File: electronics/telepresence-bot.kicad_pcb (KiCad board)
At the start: 4 copper layers, 100 x 100 mm, 191 parts, among them J1 STATUS, J10 Conn_01x02_Pin, J12 GND, J13 Conn_01x08_Pin, J14 IOLV / VIO, J15 Conn_02x06_Counter_Clockwise, J16 MOT_CON, J17 Conn_02x06_Counter_Clockwise, J18 MOT_CON, J19 Conn_02x06_Counter_Clockwise, J2 EXT_PWR_BTN, J20 MOT_CON, J3 IOLV_IN, J4 BATT, J5 BATT_OUT, J6 Conn_02x06_Counter_Clockwise, J7 MOT_CON, J8 VMOT, J9 BP_MOTOR_ENABLE, Q1 Q_PMOS_GDS, Q2 PMOS_GDS, Q3 2N3904, Q4 2N3904, U10 ISO7762DBQ, U11 LM1117DT-3.3, U12 SFH617A-1, U13 BTT TMC5160 Pro, U14 BTT TMC5160 Pro, U15 BTT TMC5160 Pro, U2 LM1117DT-5.0, U3 LM1117DT-3.3, U4 SFH617A-1, U5 DBG_HDR, U6 INA228, U7 BTT TMC5160 Pro, U8 SFH617A-1, U9 74LVC125

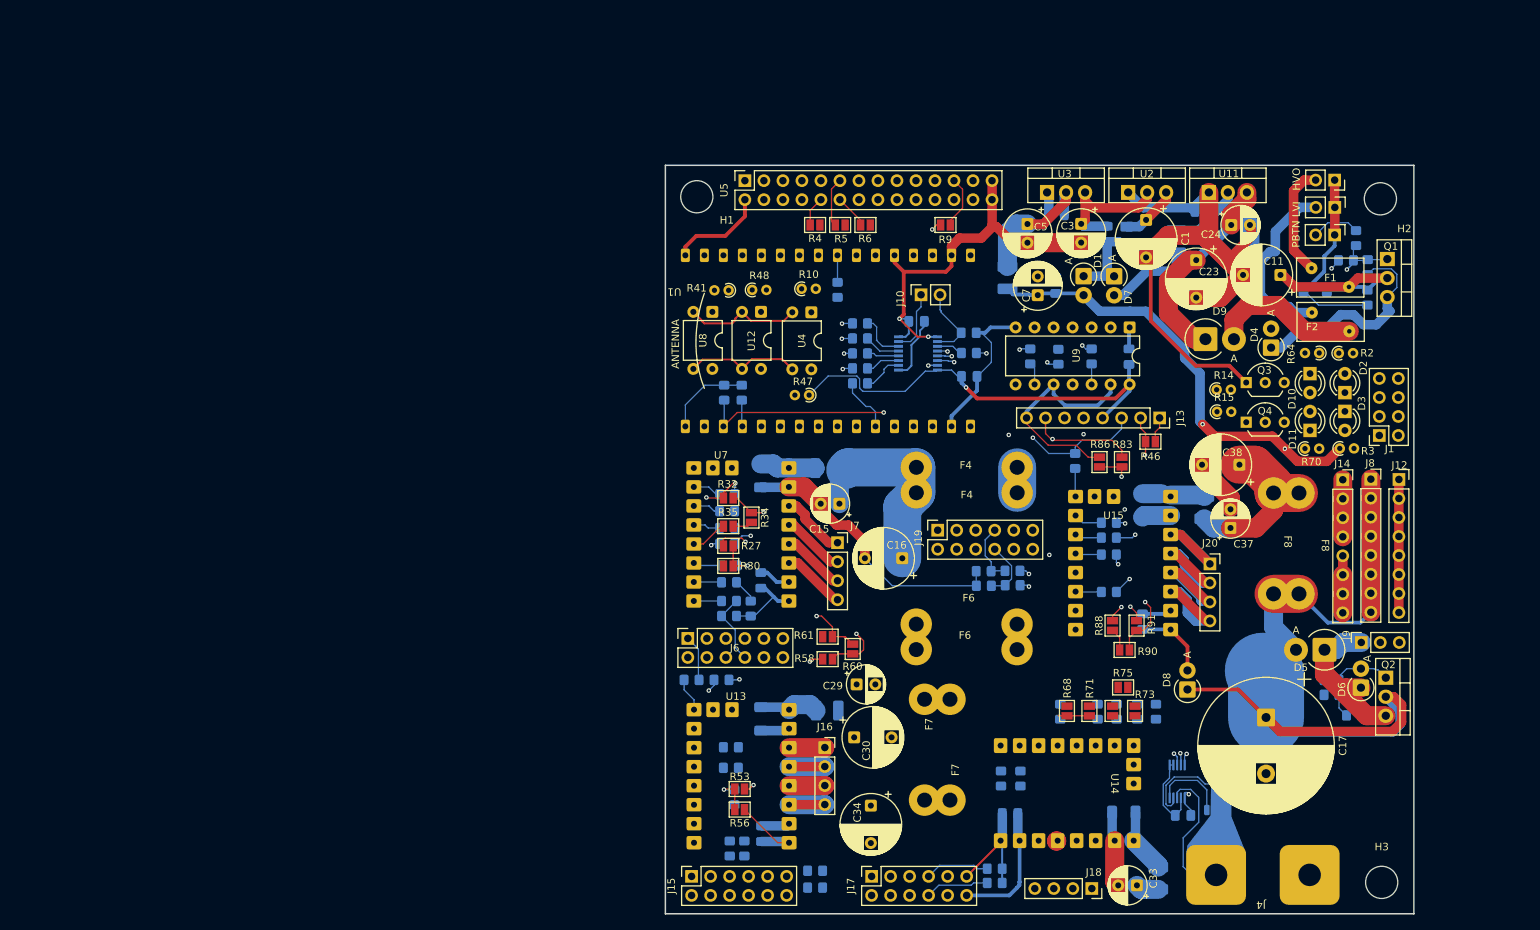
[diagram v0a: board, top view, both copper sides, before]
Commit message: Switching to a bigger PCB since cost seems negligible
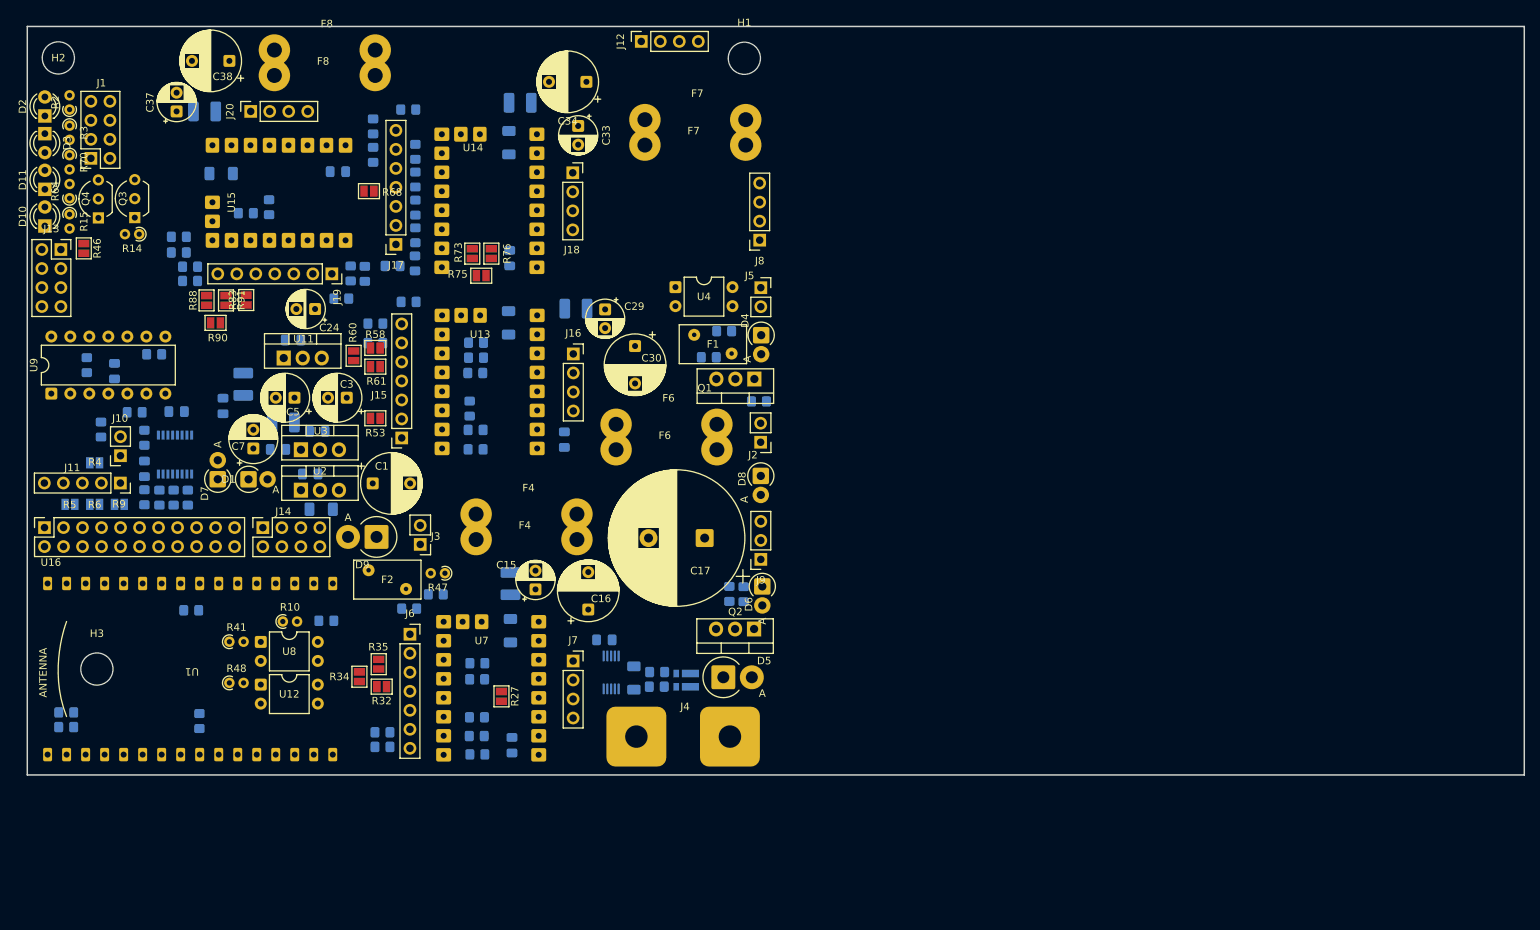
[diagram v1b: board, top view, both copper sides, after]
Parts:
- removed C11, C23: 100uF, Capacitor_THT:CP_Radial_D8.0mm_P5.00mm
- removed C12: 100nF, Capacitor_SMD:C_1206_3216Metric_Pad1.33x1.80mm_HandSolder
- removed R56, R71, R86: 0, Jumper:SolderJumper-2_P1.3mm_Open_Pad1.0x1.5mm
- removed U5: DBG_HDR, Connector_PinSocket_2.54mm:PinSocket_2x14_P2.54mm_Vertical
- added C10: 100nF, Capacitor_SMD:C_1206_3216Metric_Pad1.33x1.80mm_HandSolder, B.Cu at (146.3, 118.5)
- added J11: DRIVER_GPIO, Connector_PinSocket_2.54mm:PinSocket_1x05_P2.54mm_Vertical, F.Cu at (77.7, 92.5)
- added U16: DBG_HDR, Connector_PinSocket_2.54mm:PinSocket_2x11_P2.54mm_Vertical, F.Cu at (67.5, 98.4)
- J12, J8: footprint Connector_PinSocket_2.54mm:PinSocket_1x08_P2.54mm_Vertical -> Connector_PinSocket_2.54mm:PinSocket_1x04_P2.54mm_Vertical
- J13, J14: footprint Connector_PinSocket_2.54mm:PinSocket_1x08_P2.54mm_Vertical -> Connector_PinSocket_2.54mm:PinSocket_2x04_P2.54mm_Vertical
- J15, J17, J19, J6: value Conn_02x06_Counter_Clockwise -> Conn_01x07_Pin; footprint Connector_PinSocket_2.54mm:PinSocket_2x06_P2.54mm_Vertical -> Connector_PinSocket_2.54mm:PinSocket_1x07_P2.54mm_Vertical
- R12: value 100k -> 33R
- R22: footprint Resistor_SMD:R_Shunt_Vishay_WSK2512_6332Metric_T2.66mm -> Resistor_SMD:R_Shunt_Vishay_WSKW0612
- R30: value 0 -> 33R; footprint Jumper:SolderJumper-2_P1.3mm_Open_Pad1.0x1.5mm -> Resistor_SMD:R_0805_2012Metric_Pad1.20x1.40mm_HandSolder; moved to B.Cu
- R4, R5, R6, R9: moved to B.Cu
- moved H2 177.6 mm to (69.4, 35.6)
- moved D3 177.6 mm to (67.6, 45.8)
- moved D2 177.6 mm to (67.6, 43.4)
- moved J1 176.1 mm to (73.8, 49.1)
- moved R3 175.1 mm to (70.9, 44.7), turned to -90 degrees
- moved H3 174.0 mm to (74.5, 117.3)
- moved R2 172.7 mm to (70.9, 42.5), turned to 90 degrees
- moved D11 172.1 mm to (67.6, 53.2)
- moved D10 170.2 mm to (67.6, 58.1), turned to 90 degrees
- moved R70 169.6 mm to (70.9, 48.6), turned to -90 degrees
- moved R64 168.2 mm to (70.9, 54.4), turned to 90 degrees
- moved Q4 155.8 mm to (74.8, 57.0), turned to 90 degrees
- moved R15 155.6 mm to (70.9, 56.5), turned to -90 degrees
- moved C37 151.4 mm to (85.2, 42.8)
- moved Q3 150.1 mm to (79.6, 57.0), turned to 90 degrees
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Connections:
- J15 pad 1: /drivers/DRV_ENABLE_ISO -> /drivers/motor_driver/_CLK_DCO
- J15 pad 2: /drivers/motor_driver/_MOSI -> /drivers/motor_driver/_MISO
- J15 pad 3: /drivers/DRV_SCK_ISO -> Net-(J15-Pin_3)
- J15 pad 4: /drivers/DRV_CS_ISO -> Net-(J15-Pin_4)
- J15 pad 5: /drivers/motor_driver/_MISO -> /drivers/motor_driver/_MOSI
- J15 pad 6: /drivers/motor_driver/_CLK_DCO -> /drivers/motor_driver/_DIR
- J17 pad 1: /drivers/DRV_ENABLE_ISO -> /drivers/motor_driver2/_CLK_DCO
- J17 pad 2: /drivers/motor_driver2/_MOSI -> /drivers/motor_driver2/_MISO
- J17 pad 3: /drivers/DRV_SCK_ISO -> Net-(J17-Pin_3)
- J17 pad 4: /drivers/DRV_CS_ISO -> Net-(J17-Pin_4)
- J17 pad 5: /drivers/motor_driver2/_MISO -> /drivers/motor_driver2/_MOSI
- J17 pad 6: /drivers/motor_driver2/_CLK_DCO -> /drivers/motor_driver2/_DIR
- J19 pad 1: /drivers/DRV_ENABLE_ISO -> /drivers/motor_driver3/_CLK_DCO
- J19 pad 2: /drivers/motor_driver3/_MOSI -> /drivers/motor_driver3/_MISO
- J19 pad 3: /drivers/DRV_SCK_ISO -> Net-(J19-Pin_3)
- J19 pad 4: /drivers/DRV_CS_ISO -> Net-(J19-Pin_4)
- J19 pad 5: /drivers/motor_driver3/_MISO -> /drivers/motor_driver3/_MOSI
- J19 pad 6: /drivers/motor_driver3/_CLK_DCO -> /drivers/motor_driver3/_DIR
- J6 pad 1: /drivers/DRV_ENABLE_ISO -> /drivers/motor_driver1/_CLK_DCO
- J6 pad 2: /drivers/motor_driver1/_MOSI -> /drivers/motor_driver1/_MISO
- J6 pad 3: /drivers/DRV_SCK_ISO -> Net-(J6-Pin_3)
- J6 pad 4: /drivers/DRV_CS_ISO -> Net-(J6-Pin_4)
- J6 pad 5: /drivers/motor_driver1/_MISO -> /drivers/motor_driver1/_MOSI
- J6 pad 6: /drivers/motor_driver1/_CLK_DCO -> /drivers/motor_driver1/_DIR
- R12 pad 1: /AUX_PWR_RAIL -> Net-(U6-Vin+)
- R12 pad 2: GND -> Net-(R12-Pad2)
- R22 pad 1: +BATT -> /MOTOR_POWER_RAIL
- R22 pad 2: Net-(U6-Vin+) -> Net-(R22-Pad2)
- R22 pad 3: Net-(U6-Vin-) -> Net-(R12-Pad2)
- R22 pad 4: /MOTOR_POWER_RAIL -> +BATT
- R30 pad 1: GND -> Net-(U6-Vin-)
- R30 pad 2: /drivers/motor_driver1/_CLK_DCO -> Net-(R22-Pad2)
- U13 pad 17: Net-(J15-Pin_9) -> Net-(J15-Pin_4)
- U13 pad 18: Net-(J15-Pin_10) -> Net-(J15-Pin_3)
- U14 pad 17: Net-(J17-Pin_9) -> Net-(J17-Pin_4)
- U14 pad 18: Net-(J17-Pin_10) -> Net-(J17-Pin_3)
- U15 pad 17: Net-(J19-Pin_9) -> Net-(J19-Pin_4)
- U15 pad 18: Net-(J19-Pin_10) -> Net-(J19-Pin_3)
- U7 pad 17: Net-(J6-Pin_9) -> Net-(J6-Pin_4)
- U7 pad 18: Net-(J6-Pin_10) -> Net-(J6-Pin_3)
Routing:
- net GND: track 457.1 -> 0.00 mm, vias 2 -> 0
- net /3v3_compute: track 148.0 -> 0.00 mm, vias 3 -> 0
- net VMOT: track 135.7 -> 0.00 mm
- net /drivers/DRV_CLK_ISO: track 134.1 -> 0.00 mm, vias 3 -> 0
- net /drivers/DRV_VIO_ISO: track 107.8 -> 0.00 mm, vias 1 -> 0
- net /SDA: track 104.5 -> 0.00 mm, vias 3 -> 0
- net /drivers/DRV_ENABLE_ISO: track 101.8 -> 0.00 mm, vias 2 -> 0
- net /SCL: track 66.6 -> 0.00 mm, vias 1 -> 0
- net /drivers/DRV_MOSI_ISO: track 59.3 -> 0.00 mm, vias 2 -> 0
- net /drivers/DRV_CS_ISO: track 57.1 -> 0.00 mm, vias 3 -> 0
- net /MOTOR_POWER_RAIL: track 50.9 -> 0.00 mm
- net /drivers/DRV_SCK_ISO: track 49.9 -> 0.00 mm, vias 2 -> 0
- net /drivers/motor_driver3/_CLK_DCO: track 47.3 -> 0.00 mm, vias 2 -> 0
- net /drivers/motor_driver3/_MOSI: track 41.0 -> 0.00 mm, vias 2 -> 0
- net /IOLV_IN: track 35.6 -> 0.00 mm
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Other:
- board size 100 x 100 mm -> 200 x 100 mm
- board text removed: "HVO"
- board text removed: "LVI"
- board text removed: "PBTN"

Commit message: Updating electronics CAD post-production
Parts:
- removed R73, R75, R76, R88, R90, R91: 0, Jumper:SolderJumper-2_P1.3mm_Open_Pad1.0x1.5mm
- added C11: 100uF, Capacitor_THT:CP_Radial_D6.3mm_P2.50mm, F.Cu at (62.5, 103.2)
- added C12: 100nF, Capacitor_SMD:C_0805_2012Metric_Pad1.18x1.45mm_HandSolder, B.Cu at (112.7, 102.2)
- added D12: D_Schottky, Diode_THT:D_DO-201AD_P5.08mm_Vertical_KathodeUp, F.Cu at (119.1, 77.7)
- added H4: MountingHole_Pad_MP, MountingHole:MountingHole_4.3mm_M4_ISO7380, F.Cu at (16.4, 107.8)
- added JP1: Jumper_2_Bridged, Connector_PinSocket_2.54mm:PinSocket_1x02_P2.54mm_Vertical, F.Cu at (109.2, 107.0)
- added JP2: Jumper_2_Bridged, Connector_PinSocket_2.54mm:PinSocket_1x02_P2.54mm_Vertical, F.Cu at (109.2, 79.1)
- added R56: 0, Jumper:SolderJumper-2_P1.3mm_Open_Pad1.0x1.5mm, B.Cu at (72.3, 57.4)
- D5, D9: footprint Diode_THT:D_DO-201AD_P3.81mm_Vertical_AnodeUp -> Diode_THT:D_DO-201AD_P5.08mm_Vertical_KathodeUp
- D8: footprint Diode_THT:D_DO-41_SOD81_P2.54mm_Vertical_AnodeUp -> Diode_THT:D_DO-201AD_P5.08mm_Vertical_KathodeUp
- R32, R34, R35, R58, R60, R61: moved to B.Cu
- R41, R47: footprint Resistor_THT:R_Axial_DIN0204_L3.6mm_D1.6mm_P1.90mm_Vertical -> Resistor_THT:R_Axial_DIN0204_L3.6mm_D1.6mm_P2.54mm_Vertical
- moved J8 147.9 mm to (22.5, 14.1), turned to 0 degrees
- moved D8 135.0 mm to (50.0, 18.1)
- moved J12 133.7 mm to (14.1, 22.4), turned to 0 degrees
- moved H3 116.6 mm to (16.4, 16.3)
- moved C17 113.2 mm to (77.1, 18.4), turned to -90 degrees
- moved F7 112.8 mm to (35.9, 29.8), turned to 90 degrees
- moved Q2 111.6 mm to (105.9, 15.7), turned to 0 degrees
- moved C16 108.3 mm to (65.2, 31.2)
- moved D5 107.7 mm to (111.7, 21.3), turned to 180 degrees
- moved J7 103.9 mm to (71.0, 36.9), turned to 90 degrees
- moved R38 103.2 mm to (108.6, 18.4), turned to 180 degrees
- moved R40 102.4 mm to (113.3, 15.6), turned to -90 degrees
- moved J9 100.4 mm to (115.6, 14.3), turned to 0 degrees
- moved R22 99.4 mm to (115.5, 26.8), turned to -90 degrees
- moved C13 97.3 mm to (81.5, 43.2), turned to 180 degrees
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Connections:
- C1 pad 1: /IOLV_IN -> Net-(D12-K)
- C2 pad 1: /IOLV_IN -> Net-(D12-K)
- J13 pad 5: /drivers/DRV_SCK_ISO -> Net-(J13-Pin_5)
- J13 pad 6: /drivers/DRV_CS_ISO -> Net-(J13-Pin_6)
- J13 pad 7: /drivers/DRV_CLK_ISO -> Net-(J13-Pin_7)
- J15 pad 1: /drivers/motor_driver/_CLK_DCO -> Net-(J15-Pin_1)
- J15 pad 2: /drivers/motor_driver/_MISO -> Net-(J15-Pin_2)
- J15 pad 3: Net-(J15-Pin_3) -> /drivers/DRV_MOSI_ISO
- J15 pad 4: Net-(J15-Pin_4) -> /drivers/motor_driver/_MISO
- J15 pad 5: /drivers/motor_driver/_MOSI -> /drivers/motor_driver/_CLK_DCO
- J15 pad 6: /drivers/motor_driver/_DIR -> /drivers/motor_driver/_STEP
- J15 pad 7: /drivers/motor_driver/_STEP -> /drivers/motor_driver/_DIR
- J17 pad 1: /drivers/motor_driver2/_CLK_DCO -> Net-(J17-Pin_1)
- J17 pad 2: /drivers/motor_driver2/_MISO -> Net-(J17-Pin_2)
- J17 pad 3: Net-(J17-Pin_3) -> /drivers/motor_driver1/_MISO
- J17 pad 4: Net-(J17-Pin_4) -> /drivers/motor_driver2/_MISO
- J17 pad 5: /drivers/motor_driver2/_MOSI -> /drivers/motor_driver2/_CLK_DCO
- J17 pad 6: /drivers/motor_driver2/_DIR -> /drivers/motor_driver2/_STEP
- J17 pad 7: /drivers/motor_driver2/_STEP -> /drivers/motor_driver2/_DIR
- J19 pad 1: /drivers/motor_driver3/_CLK_DCO -> Net-(J19-Pin_1)
- J19 pad 2: /drivers/motor_driver3/_MISO -> Net-(J19-Pin_2)
- J19 pad 3: Net-(J19-Pin_3) -> /drivers/motor_driver2/_MISO
- J19 pad 4: Net-(J19-Pin_4) -> /drivers/DRV_MOSI_LAST
- J19 pad 5: /drivers/motor_driver3/_MOSI -> /drivers/motor_driver3/_CLK_DCO
- J19 pad 6: /drivers/motor_driver3/_DIR -> /drivers/motor_driver3/_STEP
- J19 pad 7: /drivers/motor_driver3/_STEP -> /drivers/motor_driver3/_DIR
- J6 pad 1: /drivers/motor_driver1/_CLK_DCO -> Net-(J6-Pin_1)
- J6 pad 2: /drivers/motor_driver1/_MISO -> Net-(J6-Pin_2)
- J6 pad 3: Net-(J6-Pin_3) -> /drivers/motor_driver/_MISO
- J6 pad 4: Net-(J6-Pin_4) -> /drivers/motor_driver1/_MISO
- J6 pad 5: /drivers/motor_driver1/_MOSI -> /drivers/motor_driver1/_CLK_DCO
- J6 pad 6: /drivers/motor_driver1/_DIR -> /drivers/motor_driver1/_STEP
- J6 pad 7: /drivers/motor_driver1/_STEP -> /drivers/motor_driver1/_DIR
- R25 pad 1: /drivers/motor_driver1/_MOSI -> /drivers/motor_driver/_MISO
- R32 pad 1: /drivers/motor_driver/MISO -> /drivers/DRV_CLK_ISO
- R32 pad 2: /drivers/motor_driver1/_MOSI -> Net-(J13-Pin_7)
- R34 pad 1: /drivers/motor_driver/MISO -> /drivers/DRV_CS_ISO
- R34 pad 2: /drivers/motor_driver1/MISO -> Net-(J13-Pin_6)
- R35 pad 1: /drivers/motor_driver1/MISO -> /drivers/DRV_SCK_ISO
- R35 pad 2: /drivers/motor_driver1/_MISO -> Net-(J13-Pin_5)
- R36 pad 1: /drivers/motor_driver1/_STEP -> GND
- R36 pad 2: GND -> Net-(U7-STEP)
- R37 pad 1: /drivers/motor_driver1/_DIR -> GND
- R37 pad 2: GND -> Net-(U7-DIR)
- R51 pad 1: /drivers/motor_driver/_MOSI -> /drivers/DRV_MOSI_ISO
- R58 pad 2: /drivers/motor_driver/_MOSI -> /drivers/motor_driver/_MISO
- R60 pad 1: /drivers/DRV_MOSI_ISO -> /drivers/motor_driver1/_MISO
- R60 pad 2: /drivers/motor_driver/MISO -> /drivers/motor_driver2/_MISO
- R61 pad 1: /drivers/motor_driver/MISO -> /drivers/motor_driver2/_MISO
- R61 pad 2: /drivers/motor_driver/_MISO -> /drivers/DRV_MOSI_LAST
- R62 pad 1: /drivers/motor_driver/_STEP -> GND
- R62 pad 2: GND -> Net-(U13-STEP)
- R63 pad 1: /drivers/motor_driver/_DIR -> GND
- R63 pad 2: GND -> Net-(U13-DIR)
- R66 pad 1: /drivers/motor_driver2/_MOSI -> /drivers/motor_driver1/_MISO
- R77 pad 1: /drivers/motor_driver2/_STEP -> GND
- R77 pad 2: GND -> Net-(U14-STEP)
- R78 pad 1: /drivers/motor_driver2/_DIR -> GND
- R78 pad 2: GND -> Net-(U14-DIR)
- R81 pad 1: /drivers/motor_driver3/_MOSI -> /drivers/motor_driver2/_MISO
- R92 pad 1: /drivers/motor_driver3/_STEP -> GND
- R92 pad 2: GND -> Net-(U15-STEP)
- R93 pad 1: /drivers/motor_driver3/_DIR -> GND
- R93 pad 2: GND -> Net-(U15-DIR)
- U1 pad 1: /3v3_compute -> Net-(JP1-B)
- U1 pad 14: /5v_compute -> Net-(JP2-B)
- U13 pad 17: Net-(J15-Pin_4) -> Net-(J15-Pin_2)
- U13 pad 18: Net-(J15-Pin_3) -> Net-(J15-Pin_1)
- U14 pad 17: Net-(J17-Pin_4) -> Net-(J17-Pin_2)
- U14 pad 18: Net-(J17-Pin_3) -> Net-(J17-Pin_1)
- U15 pad 17: Net-(J19-Pin_4) -> Net-(J19-Pin_2)
- U15 pad 18: Net-(J19-Pin_3) -> Net-(J19-Pin_1)
- U15 pad 5: /drivers/motor_driver3/_MISO -> /drivers/DRV_MOSI_LAST
- U2 pad 3: /IOLV_IN -> Net-(D12-K)
- U7 pad 17: Net-(J6-Pin_4) -> Net-(J6-Pin_2)
- U7 pad 18: Net-(J6-Pin_3) -> Net-(J6-Pin_1)
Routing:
- net GND: track 0.00 -> 545.0 mm, vias 0 -> 98
- net /drivers/DRV_VIO_ISO: track 0.00 -> 249.0 mm, vias 0 -> 1
- net /3v3_compute: track 0.00 -> 232.4 mm, vias 0 -> 6
- net /5v_compute: track 0.00 -> 209.2 mm
- net /drivers/DRV_ENABLE_ISO: track 0.00 -> 137.7 mm, vias 0 -> 4
- net /drivers/DRV_SCK_ISO: track 0.00 -> 136.4 mm, vias 0 -> 6
- net /drivers/DRV_CS_ISO: track 0.00 -> 135.0 mm, vias 0 -> 6
- net /drivers/DRV_CLK_ISO: track 0.00 -> 124.6 mm, vias 0 -> 7
- net /IOLV_IN: track 0.00 -> 119.0 mm, vias 0 -> 1
- net /SDA: track 0.00 -> 114.5 mm, vias 0 -> 1
- net /SCL: track 0.00 -> 109.8 mm, vias 0 -> 2
- net /MOTOR_POWER_RAIL: track 0.00 -> 95.7 mm
- net /BATT_ALERT: track 0.00 -> 95.6 mm, vias 0 -> 3
- net VMOT: track 0.00 -> 84.0 mm
- net Net-(D6-A): track 0.00 -> 80.4 mm, vias 0 -> 1
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- added copper zone on B.Cu, net +BATT
- added copper zone on F.Cu, net +BATT
- added copper zone on In1.Cu, net +BATT
- added copper zone on In2.Cu, net +BATT
- added copper zone on B.Cu, net /MOTOR_POWER_RAIL
- added copper zone on F.Cu, net /MOTOR_POWER_RAIL
- added copper zone on In1.Cu, net /MOTOR_POWER_RAIL
- added copper zone on In2.Cu, net /MOTOR_POWER_RAIL
- added copper zone on B.Cu, net GND
- added copper zone on F.Cu, net GND
- added copper zone on In1.Cu, net GND
- added copper zone on In2.Cu, net GND
- added copper zone on B.Cu, net VMOT
- added copper zone on F.Cu, net VMOT
- added copper zone on In1.Cu, net VMOT
- added copper zone on In2.Cu, net VMOT
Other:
- board size 200 x 100 mm -> 116 x 100 mm
- board text added: "3v3 DRV GND 5v0 GND 5v0 5v0 HVE"
- board text added: "3v3 ISOLATE"
- board text added: "3v3 PWR"
- board text added: "5V-ISOLATE"
- board text added: "5v PWR"
- board text added: "AUX"
- board text added: "BP_0"
- board text added: "BP_1"
- board text added: "BP_2"
- board text added: "BP_3"
- board text added: "CLK DBG"
- board text added: "CLK_DBG"
- board text added: "CS_DBG CLK_DBG SCK_DBG"
- board text added: "DRV EN"
- board text added: "DRV0"
- board text added: "DRV1"
- board text added: "DRV2"
- board text added: "DRV3"
- board text added: "ESP32 C6 DevKitC v1"
- board text added: "GND"
- board text added: "HV EN"
- board text added: "IOLV"
- board text added: "JLCJLCJLCJLC"
- board text added: "LVI"
- board text added: "PBTN"
- board text added: "SCK_DBG"
- board text added: "SDI_DBG"
- board text added: "SDO_DBG"
- board text added: "VIO_ISO"
- board text added: "VMOT"
- board text added: "Yash's Things! https://devya.sh"
